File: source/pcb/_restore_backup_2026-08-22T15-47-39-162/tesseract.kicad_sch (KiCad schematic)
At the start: 83 parts, among them J1 USB_C_Receptacle_USB2.0_14P, J2 AudioJack3_SwitchTR, J3 Conn_01x12, J4 Conn_01x02, J5 Micro_SD_Card_Det1, SW1 SW_Push, SW2 SW_Push, SW3 SW_Push, SW4 SW_Push, SW5 SW_Push, SW6 SW_Push, U1 PCM5102A, U2 IP5306, U3 RP2354A, U4 XC6206PxxxMR, U5 PAM8403D, Y1 Crystal_GND24

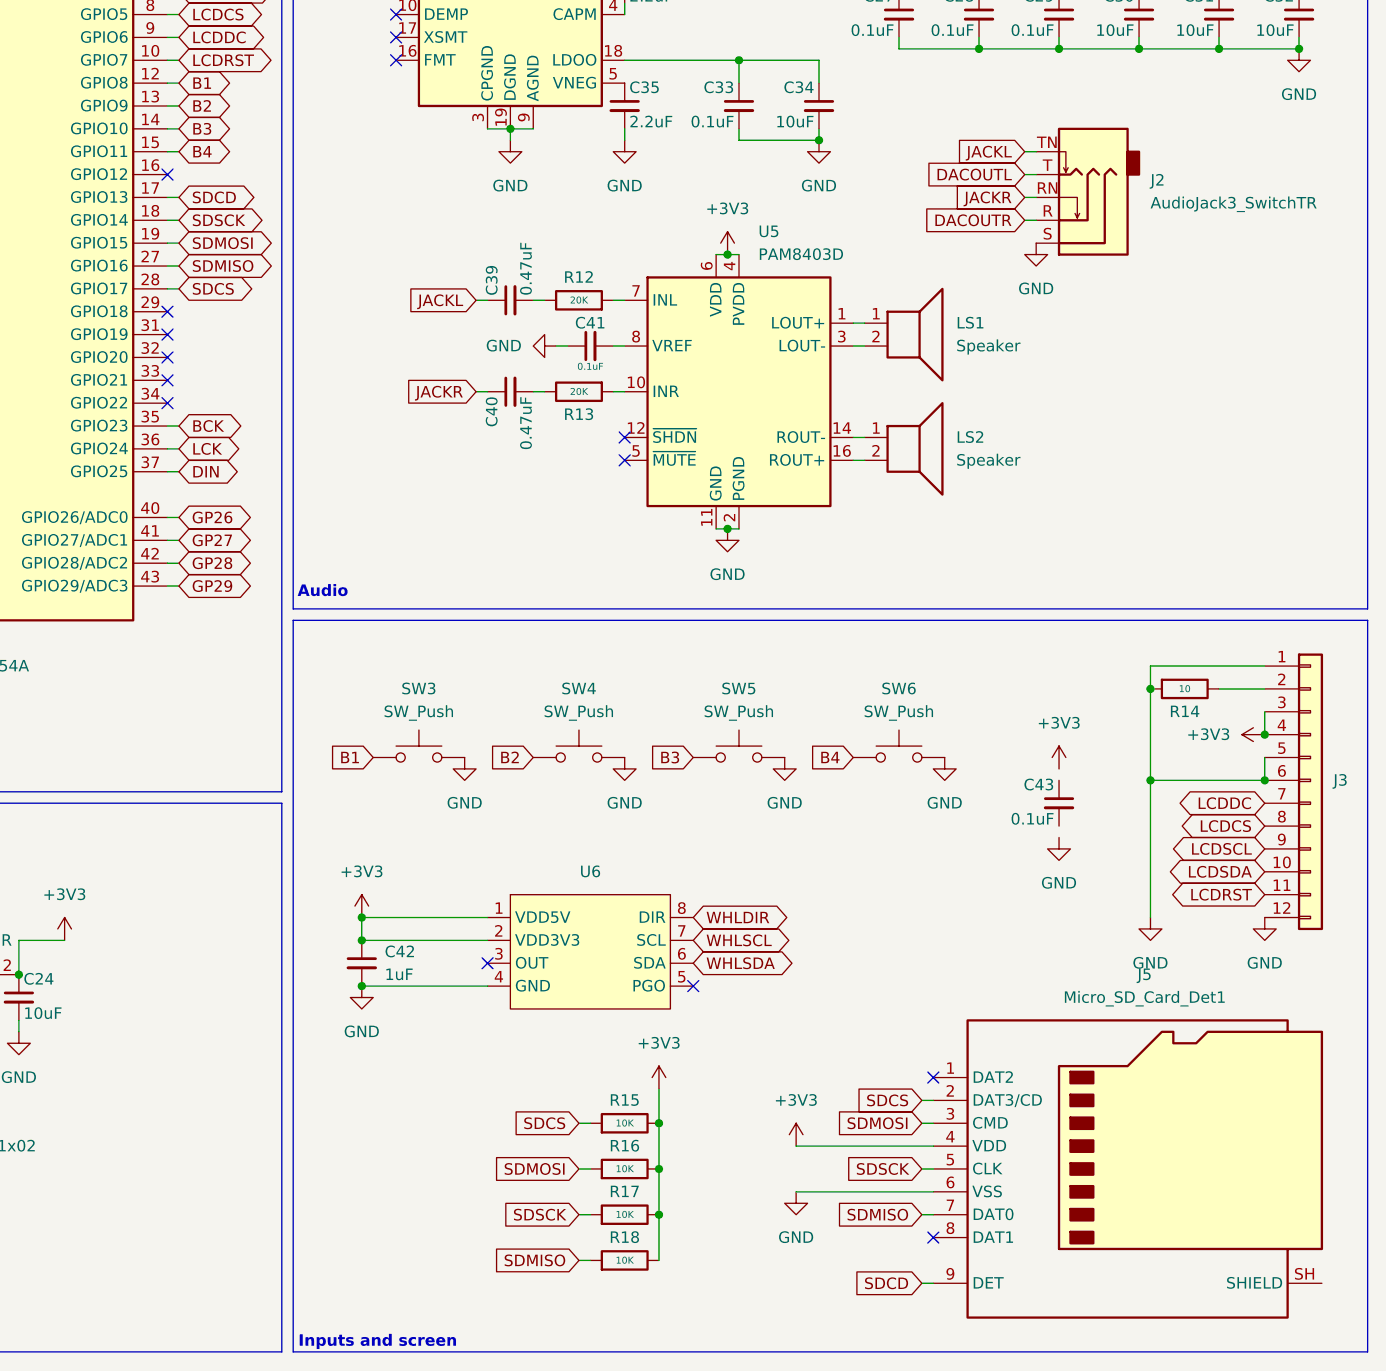
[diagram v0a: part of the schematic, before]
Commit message: Added microSD card to schematic
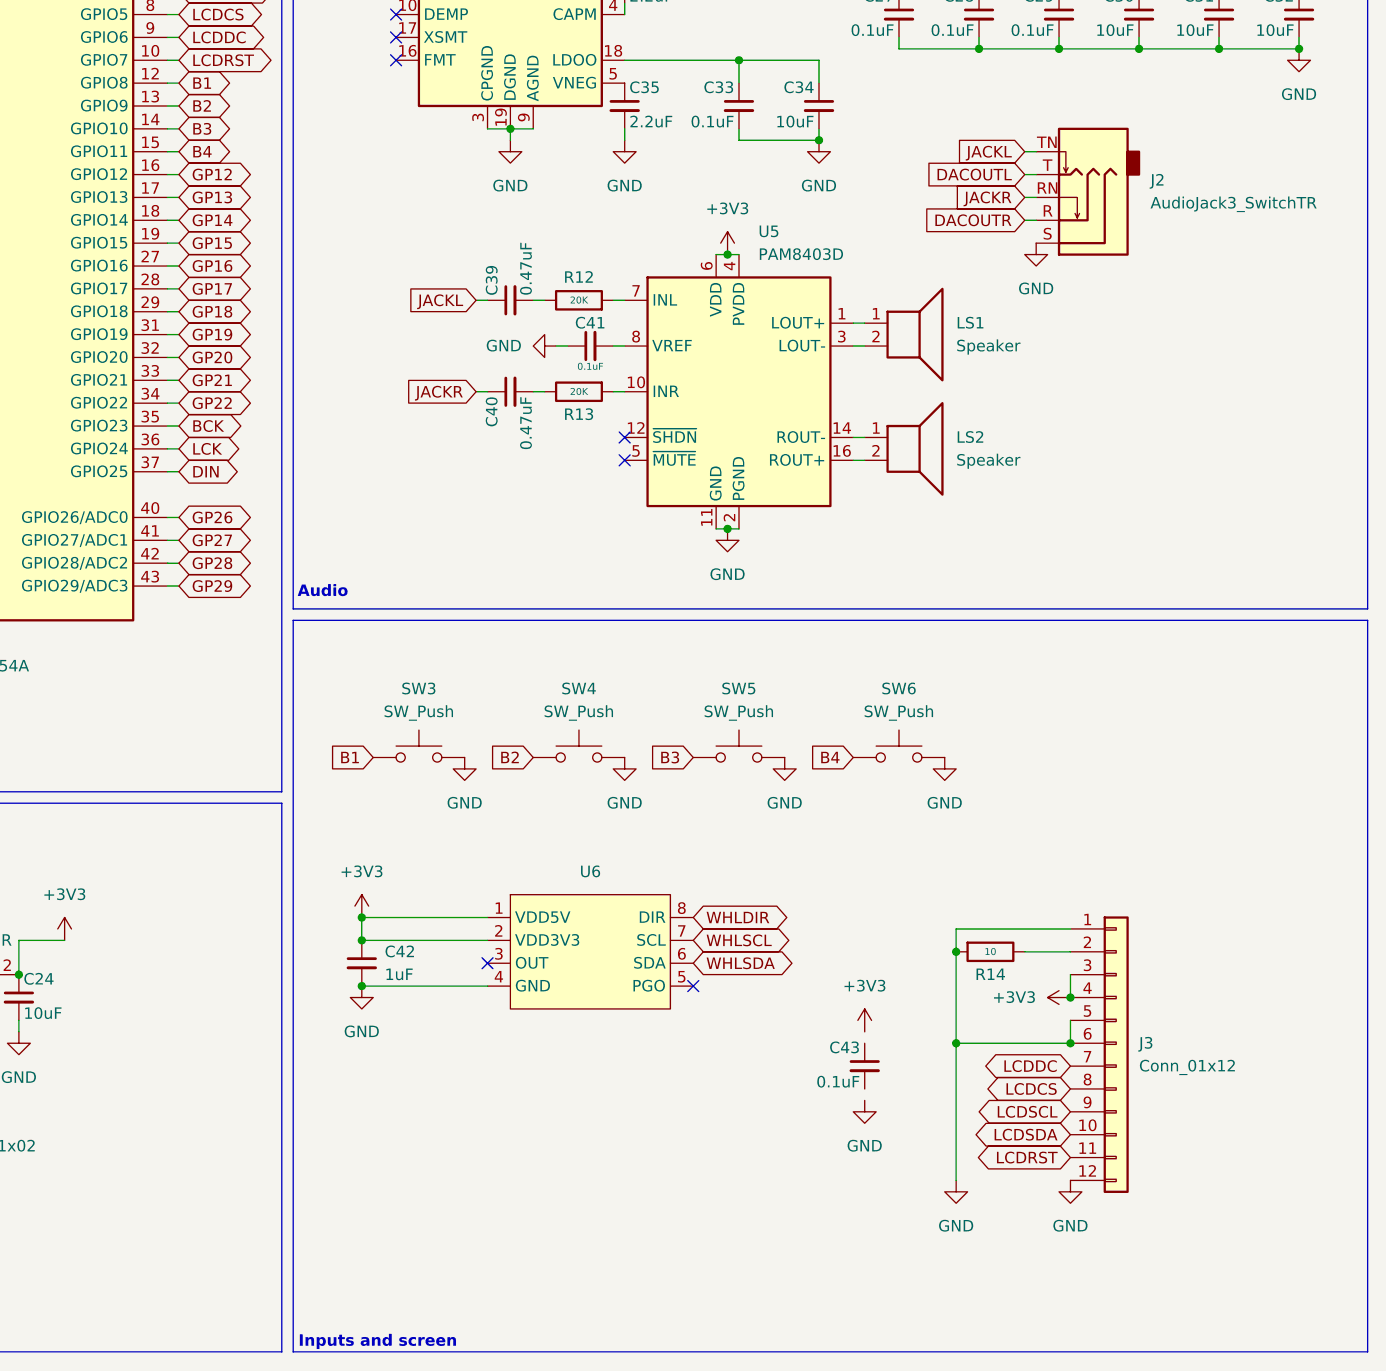
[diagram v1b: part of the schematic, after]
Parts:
- removed J5: Micro_SD_Card_Det1, Connector_Card:microSD_HC_Hirose_DM3BT-DSF-PEJS, symbol KiCad:Micro_SD_Card_Det1
- removed R15, R16, R17, R18: 10K, Resistor_SMD:R_0402_1005Metric, symbol Device:R
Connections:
- net GP12: now reaches U3.16 (GPIO12)
- net GP18: now reaches U3.29 (GPIO18)
- net GP19: now reaches U3.31 (GPIO19)
- net GP20: now reaches U3.32 (GPIO20)
- net GP21: now reaches U3.33 (GPIO21)
- net GP22: now reaches U3.34 (GPIO22)
- net SDCD renamed GP13
- net SDCS renamed GP17
- net SDMISO renamed GP16
- net SDMOSI renamed GP15
- net SDSCK renamed GP14
- no-connect marks 26 -> 18
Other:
- moved on the sheet: C43, J3, R14
